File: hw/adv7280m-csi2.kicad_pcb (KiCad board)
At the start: 4 copper layers, 42 x 55 mm, 72 parts, among them J1 RPi_CSI_15pin, J2 CVBS_RCA, J4 5V_IN, J5 CVBS_IN_HDR, J6 MON1_HDR, J7 MON2_HDR, J8 CVBS_BUF_HDR, U1 ADV7280WBCPZ-M, U2 AP2112K-1.8, U3 AP2112K-1.8, U5 THS7314DR, Y1 28.63636MHz

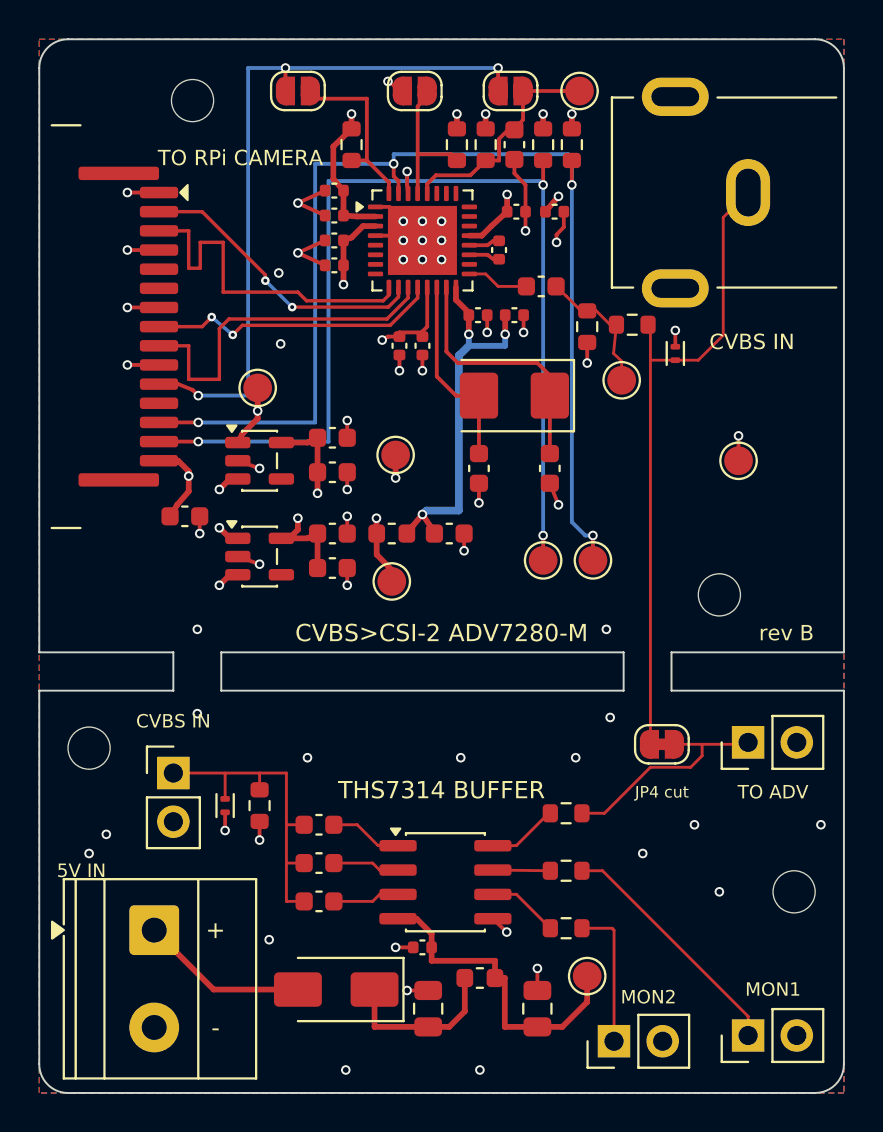
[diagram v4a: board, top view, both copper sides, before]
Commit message: Rev C (SPRUT-2 case): one board, JST connectors, final routing, fab outputs
Board and parts
- One solid 42x55 mm board (no breakaway section); JST-PH video in/out (J5 in,
  J6 TV, J7 GX16) and JST-XH 5 V (J4) on the edges; buffer CH1 hard-wired to the
  decoder input (RCA J2, J8, JP4, D1 removed).
- U1 ADV7280BCPZ-M (C662255) assembled by JLCPCB; LDO input caps C29/C30 1 uF.
- KiCad 10 on Windows: generator paths, field transfer for KiCad 10 DRC,
  portable fab.sh, .gitattributes keeps *.sh LF.

Routing (docs/routing-rules.md, audit items 1-18)
- MIPI CSI-2 as loosely coupled pairs 0.30/0.45 mm (101 R diff, 29 R common
  mode); both lines of each pair get 2 vias, GND return vias at every layer
  change, lengths matched (P = N, 0.2 mm between pairs).
- In2 GND everywhere with compact power zones; every B.Cu signal (MIPI hops,
  I2C, CAM_GPIO) runs over one plane; CAM_GPIO clears the H1 mounting hole.
- Video 75 R: 0.13 mm with a 0.4 mm pour gap (hw/adv7280m-csi2.kicad_dru).
- Crystal turned 90 deg right under pins 14/15 (XTALN 2.8 mm), load caps at
  its pads, nothing under it; 10 nF next to every supply pin, plane after the
  100 nF; PVDD feed on B.Cu around the crystal.
- U1 exposed pad: own footprint with 4 paste windows (60 %) and 5 vias
  0.45/0.2 mm in the paste-free cross.
- ERC 0, check_nets OK, DRC (all severities, schematic parity) 0/0/0.

Docs and outputs
- Gerber/drill, JLCPCB BOM/CPL, schematic PDF/PNG, renders, layer images,
  STEP/DXF regenerated; assumptions A6-1..A6-16; docs/bring-up.md (first
  power-up to ustreamer); tools/zsolve.py impedance solver.

Co-Authored-By: Claude Opus 5.5 <noreply@anthropic.com>
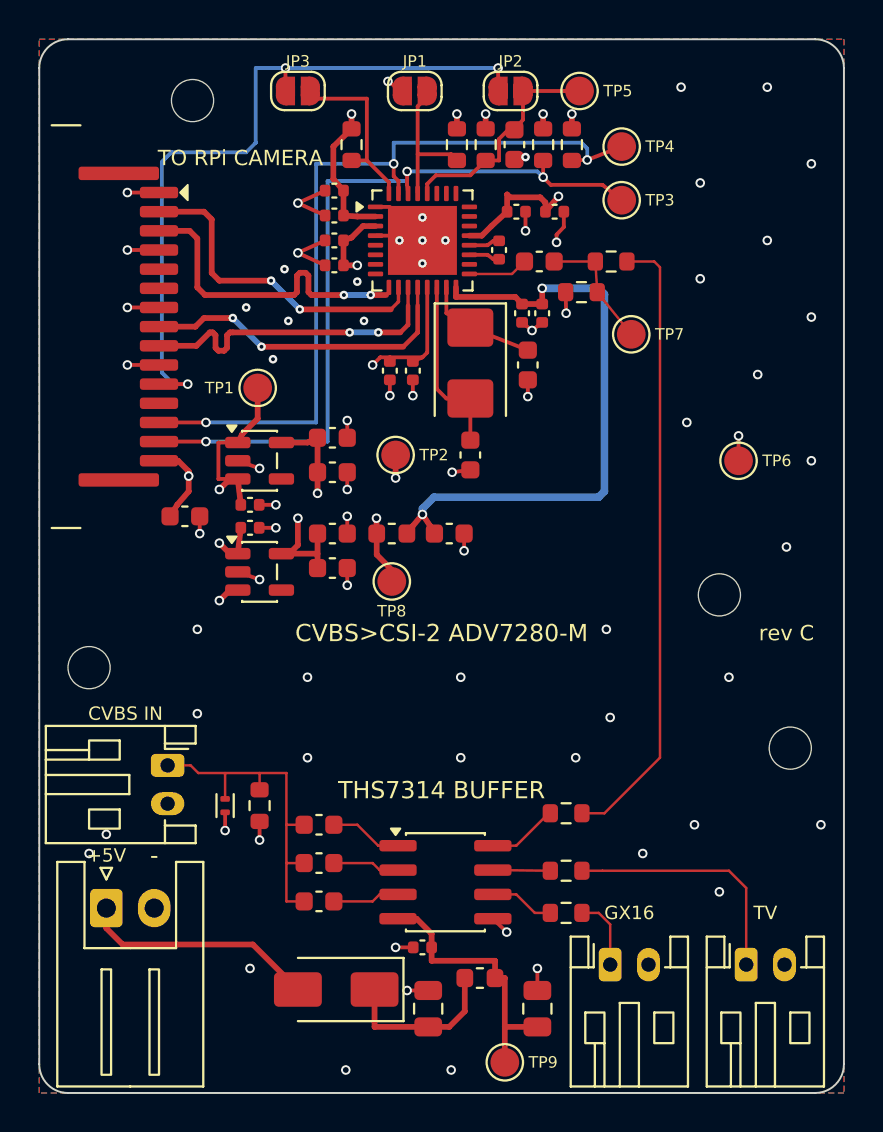
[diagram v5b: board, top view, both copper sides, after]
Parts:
- removed D1: TPD1E10B06, adv-parts:TI_X1SON-2_DPY0002A_1.0x0.6mm
- removed J2: CVBS_RCA, adv-parts:RCA_Multicomp_PSG01546_Horizontal
- removed J8: CVBS_BUF_HDR, Connector_PinHeader_2.54mm:PinHeader_1x02_P2.54mm_Vertical
- removed JP4: BUF>ADV, Jumper:SolderJumper-2_P1.3mm_Bridged_RoundedPad1.0x1.5mm
- added C29: 1uF, Capacitor_SMD:C_0402_1005Metric, F.Cu at (11.0, 24.3)
- added C30: 1uF, Capacitor_SMD:C_0402_1005Metric, F.Cu at (11.0, 25.5)
- J4: footprint TerminalBlock_Phoenix:TerminalBlock_Phoenix_MKDS-1,5-2-5.08_1x02_P5.08mm_Horizontal -> Connector_JST:JST_XH_S2B-XH-A_1x02_P2.50mm_Horizontal
- J5: value CVBS_IN_HDR -> CVBS_IN; footprint Connector_PinHeader_2.54mm:PinHeader_1x02_P2.54mm_Vertical -> Connector_JST:JST_PH_S2B-PH-K_1x02_P2.00mm_Horizontal
- J6: value MON1_HDR -> TV; footprint Connector_PinHeader_2.54mm:PinHeader_1x02_P2.54mm_Vertical -> Connector_JST:JST_PH_S2B-PH-K_1x02_P2.00mm_Horizontal
- J7: value MON2_HDR -> GX16; footprint Connector_PinHeader_2.54mm:PinHeader_1x02_P2.54mm_Vertical -> Connector_JST:JST_PH_S2B-PH-K_1x02_P2.00mm_Horizontal
- U1: value ADV7280WBCPZ-M -> ADV7280BCPZ-M; footprint Package_DFN_QFN:QFN-32-1EP_5x5mm_P0.5mm_EP3.6x3.6mm -> adv-parts:QFN-32-1EP_5x5mm_P0.5mm_EP3.6x3.6mm_Paste4
- moved TP4 21.7 mm to (30.4, 5.60)
- moved TP3 19.2 mm to (30.4, 8.40)
- moved H4 7.50 mm to (39.2, 37.0)
- moved TP9 6.22 mm to (24.3, 53.4)
- moved C3 5.52 mm to (25.5, 17.0)
- moved H3 4.20 mm to (2.60, 32.8)
- moved J7 4.00 mm to (29.8, 48.3), turned to 0 degrees
- moved J6 3.70 mm to (36.9, 48.3), turned to 0 degrees
- moved R1 3.48 mm to (29.9, 11.6)
- moved C21 3.35 mm to (26.2, 14.3), turned to -90 degrees
- moved Y1 2.86 mm to (22.5, 16.9), turned to -90 degrees
- moved J4 2.75 mm to (3.50, 45.4), turned to 0 degrees
- moved TP7 2.45 mm to (30.9, 15.4)
- moved C17 2.14 mm to (18.3, 17.3)
- moved C19 2.00 mm to (26.9, 9.00)
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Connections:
- net /MON1 renamed /TV_OUT
- net /MON2 renamed /GX16_OUT
- R9 pad 2: /CVBS_BUF -> /CVBS_IN
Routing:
- net /SCL: track 60.3 -> 42.1 mm, vias 4 -> 3
- net /SDA: track 56.3 -> 40.8 mm, vias 4 -> 3
- net PVDD: track 20.1 -> 32.3 mm, vias 3 -> 2
- net /CVBS_BUF: track 11.7 -> 0.00 mm
- net Net-(U1-XTALN): track 13.3 -> 6.03 mm
- net +3V3: track 21.9 -> 28.5 mm, vias 10 -> 9
- net /GX16_OUT: track 7.52 -> 3.82 mm
- net /5V_IN: track 8.78 -> 12.4 mm
- net +1V8A: track 13.4 -> 16.8 mm, vias 4 -> 3
- net /VS_BUF: track 16.9 -> 14.3 mm
- net GND: track 43.8 -> 41.5 mm, vias 59 -> 74
- net +1V8D: track 15.3 -> 17.3 mm
- net /CSI_D0N: track 15.5 -> 17.2 mm
- net /CSI_CLKP: track 18.6 -> 17.0 mm, vias 0 -> 2
- net /CSI_CLKN: track 15.4 -> 17.0 mm
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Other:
- outline, holes or cut-outs redrawn
- board text added: "+5V"
- board text added: "ADV7280M-CSI2 rev C github inestvan/adv"
- board text added: "GX16"
- board text added: "THS7314 BUFFER rev C SPRUT-2"
- board text added: "TV"
- board text added: "rev C"
- board text removed: "+"
- board text removed: "5V IN"
- board text removed: "ADV7280M-CSI2 rev B github inestvan/adv"
- board text removed: "JP4 cut"
- board text removed: "MON1"
- board text removed: "MON2"
- board text removed: "THS7314 BUFFER rev B"
- board text removed: "TO ADV"
- board text removed: "rev B"

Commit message: Rev C: breakaway buffer section, solder pads instead of JST, СПРУТ-М label
- Buffer section snaps off again: 2 mm slot at y 32..34 with two tabs
  (x 7.0..9.5 GND only, x 31.15..33.65 GND + CVBS_IN). While joined the video
  runs over the tab; when split, a coax is soldered between J8 "TO ADV"
  (buffer) and J2 "CVBS" (decoder). D1 TPD1E10B06 ESD back at the decoder input.
- No connectors on the board: J4 (5 V), J5 (CVBS in), J6 TV, J7 GX16, J2, J8
  are plated solder holes (PinHeader_1x02, 1.0 mm), not assembled, no 3D model;
  pin 1 kept in place, routing unchanged. JST parts removed from the BOM.
- Mounting holes: decoder H1 (8.0; 3.2) / H2 (39.5; 27.5), buffer
  H3 (3.2; 51.8) / H4 (39.5; 37.0) - each section diagonal.
- Silkscreen: product name "СПРУТ-М".
- ERC 0, check_nets OK, DRC (all severities, schematic parity) 0/0/0; MIPI
  lengths, In2 planes under B.Cu and 75 R video unchanged.
- Fab outputs, STEP/DXF, renders, schematic PNG, README, enclosure dims,
  bring-up guide (split + soldering steps), assumptions A6-17, A6-18.

Co-Authored-By: Claude Opus 5.5 <noreply@anthropic.com>
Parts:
- added D1: TPD1E10B06, adv-parts:TI_X1SON-2_DPY0002A_1.0x0.6mm, F.Cu at (33.5, 25.9)
- added J2: CVBS_PADS, Connector_PinHeader_2.54mm:PinHeader_1x02_P2.54mm_Vertical, F.Cu at (32.4, 28.5)
- added J8: TO_ADV_PADS, Connector_PinHeader_2.54mm:PinHeader_1x02_P2.54mm_Vertical, F.Cu at (32.4, 35.8)
- J4: footprint Connector_JST:JST_XH_S2B-XH-A_1x02_P2.50mm_Horizontal -> Connector_PinHeader_2.54mm:PinHeader_1x02_P2.54mm_Vertical
- J5, J6, J7: footprint Connector_JST:JST_PH_S2B-PH-K_1x02_P2.00mm_Horizontal -> Connector_PinHeader_2.54mm:PinHeader_1x02_P2.54mm_Vertical
- moved H3 19.0 mm to (3.20, 51.8)
- moved H2 4.27 mm to (39.5, 27.5)
- moved H4 0.30 mm to (39.5, 37.0)
- turned J4 to 90 degrees
- turned J5 to 0 degrees
- turned J6 to 90 degrees
- turned J7 to 90 degrees
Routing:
- net /CVBS_IN: track 32.7 -> 33.5 mm
- net GND: track 41.5 -> 42.2 mm, vias 74 -> 76
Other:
- outline, holes or cut-outs redrawn
- board text added: "CVBS"
- board text added: "TO ADV"
- board text added: "СПРУТ-М"

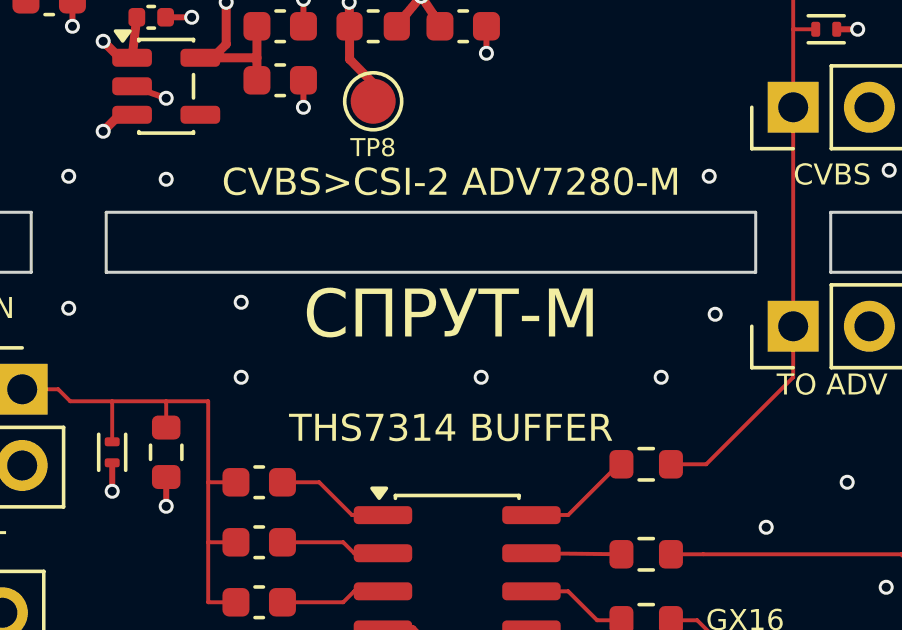
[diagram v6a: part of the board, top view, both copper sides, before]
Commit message: Rev C: Latin-only silkscreen (SPRUT-M), JLCPOST order folder
- Product name on the silkscreen changed from Cyrillic to "SPRUT-M": JLCPOST
  (order@jlcpost.ru, places the order at JLCPCB) accepts Latin only in file
  names and silkscreen. Gerber/drill/BOM/CPL and file names checked: ASCII only.
- fab/JLCPOST_SPRUT-M_rev_C/: Gerber zip, BOM, CPL, render-top.png to attach,
  ready email text (EMAIL_JLCPOST.txt) and instructions for whoever places the
  order (ORDER_JLCPCB.txt).
- DRC 0/0/0; fab outputs, renders, fab-layer DXF regenerated; assumptions A6-19.

Co-Authored-By: Claude Opus 5.5 <noreply@anthropic.com>
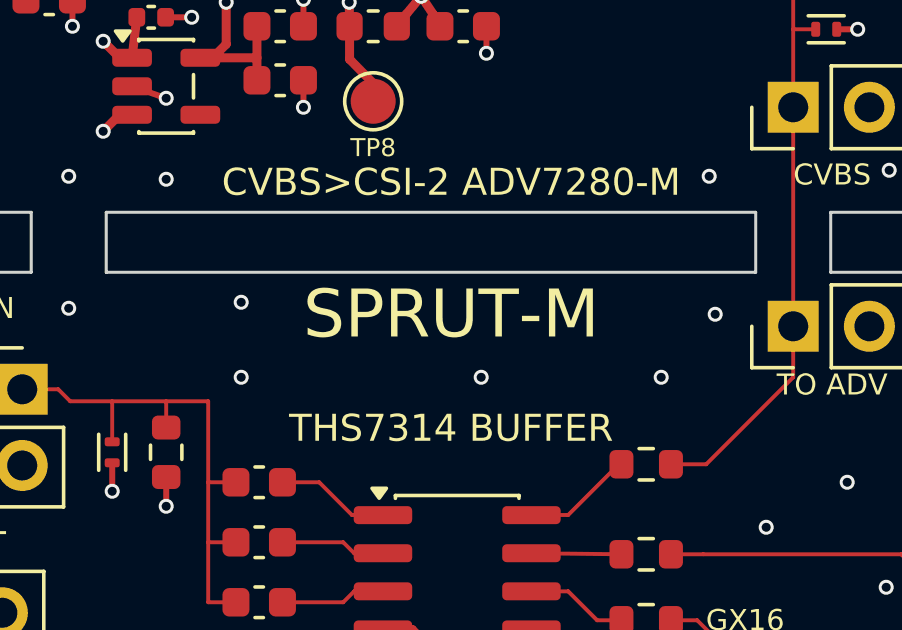
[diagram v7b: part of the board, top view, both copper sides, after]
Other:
- board text added: "SPRUT-M"
- board text removed: "СПРУТ-М"
